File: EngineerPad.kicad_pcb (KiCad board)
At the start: 2 copper layers, 114.9 x 97.8 mm, 69 parts, among them J1 AVR ISP, J2 USB_A, SW1 SW_Push, SW10 SW_Push, SW11 SW_Push, SW12 SW_Push, SW13 SW_Push, SW14 SW_Push, SW15 SW_Push, SW16 SW_Push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

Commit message: wip
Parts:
- moved C3 0.63 mm to (187.5, 79.8)
- moved F1 0.23 mm to (181.9, 79.9)
- moved D24 0.21 mm to (174.8, 81.1)
- moved D25 0.21 mm to (178.0, 81.1)
- moved D26 0.21 mm to (187.5, 73.5)
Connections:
- J1 pad 1: Row1 -> Col1
- J1 pad 3: Row0 -> Col0
- J1 pad 4: Row2 -> Col2
- U1 pad 15: Row0 -> Col4
- U1 pad 16: Row1 -> Col3
- U1 pad 17: Row2 -> Col2
- U1 pad 18: Row3 -> Col1
- U1 pad 19: Row4 -> Col0
- U1 pad 23: Col4 -> Row0
- U1 pad 24: Col3 -> Row1
- U1 pad 25: Col2 -> Row2
- U1 pad 26: Col1 -> Row3
- U1 pad 27: Col0 -> Row4
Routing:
- net +5V: track 0.00 -> 117.9 mm
- net Reset: track 0.00 -> 84.9 mm
- net D+: track 0.00 -> 33.8 mm
- net D-: track 0.00 -> 30.0 mm
- net /DN: track 0.00 -> 22.4 mm
- net /DP: track 0.00 -> 19.7 mm
- net Net-(C1-Pad2): track 0.00 -> 11.4 mm
- net Net-(C2-Pad2): track 0.00 -> 10.2 mm
- net Net-(F1-Pad2): track 0.00 -> 6.88 mm

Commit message: handwired
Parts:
- moved D23 0.20 mm to (152.0, 138.9)
- moved D21 0.20 mm to (133.0, 138.9)
- moved U1 0.18 mm to (182.5, 128.1)
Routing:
- net Col2: track 0.00 -> 200.3 mm
- net Col0: track 0.00 -> 193.5 mm
- net Col1: track 0.00 -> 181.0 mm
- net Row0: track 0.00 -> 129.9 mm
- net Col3: track 0.00 -> 126.8 mm
- net Col4: track 0.00 -> 114.3 mm
- net Row1: track 0.00 -> 109.4 mm
- net Row3: track 0.00 -> 99.4 mm
- net Row2: track 0.00 -> 94.6 mm
- net Row4: track 0.00 -> 63.2 mm
- net Net-(D21-Pad2): track 0.00 -> 16.4 mm
- net Net-(D19-Pad2): track 0.00 -> 12.6 mm
- net Net-(D4-Pad2): track 0.00 -> 12.6 mm
- net Net-(D14-Pad2): track 0.00 -> 12.6 mm
- net Net-(D16-Pad2): track 0.00 -> 12.6 mm
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
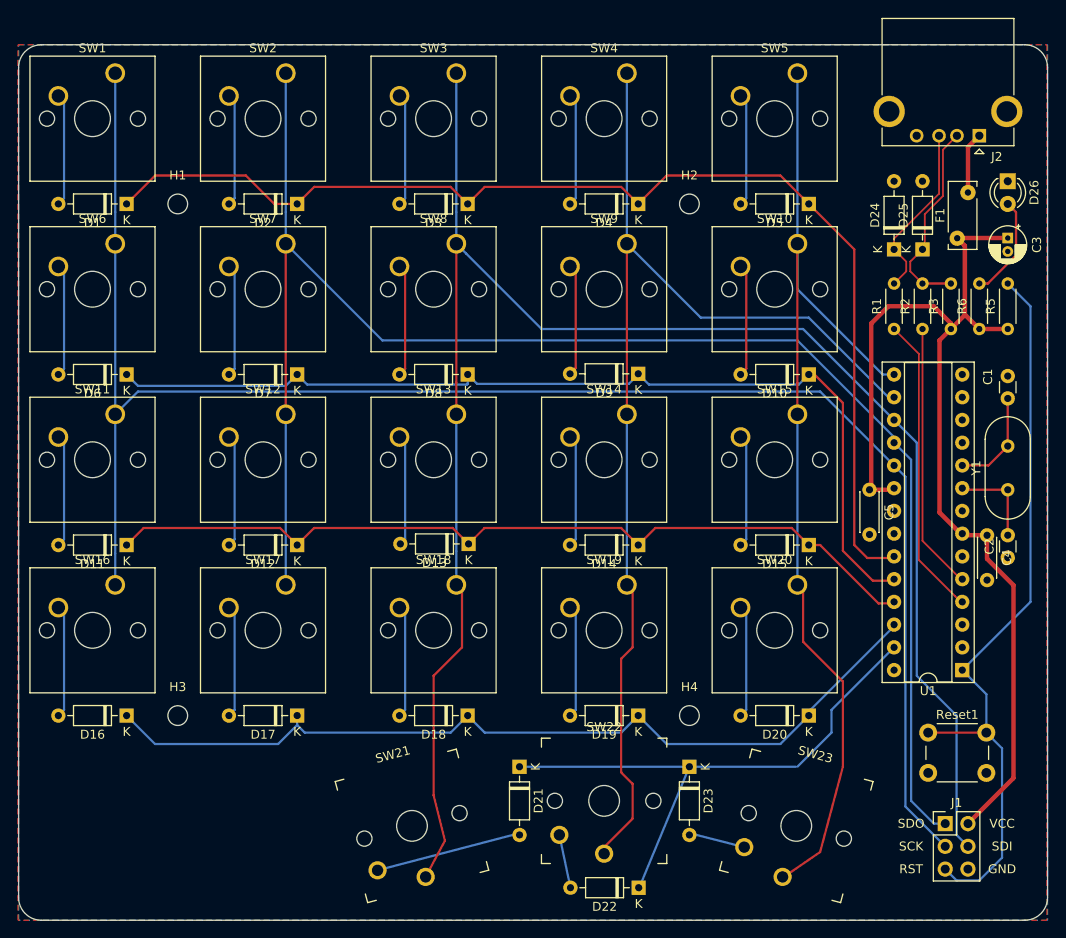
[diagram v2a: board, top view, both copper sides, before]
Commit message: fix minor wiring
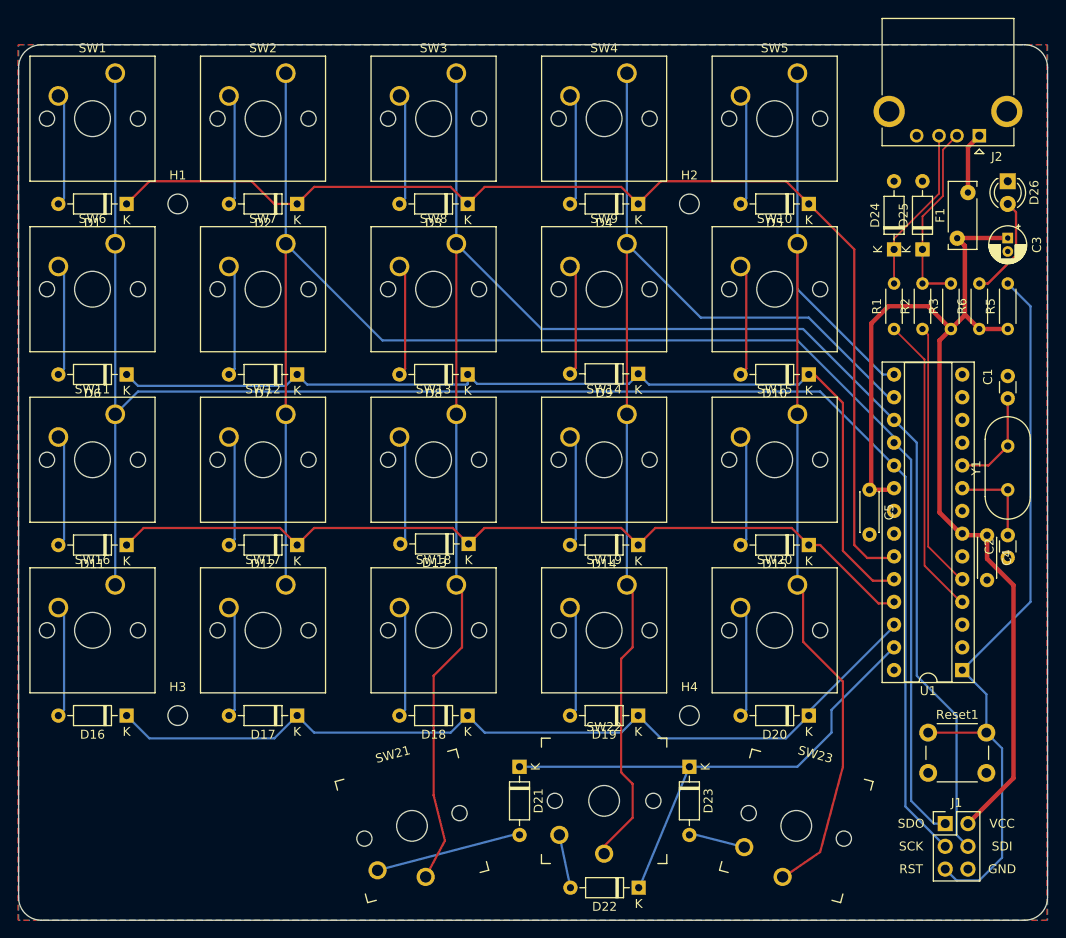
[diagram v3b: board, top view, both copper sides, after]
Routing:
- net Row3: track 99.4 -> 97.5 mm
- net /DP: track 19.7 -> 18.6 mm
- net /DN: track 22.4 -> 21.3 mm
- net Row0: track 129.9 -> 128.8 mm
- net +5V: track 118.4 -> 117.4 mm

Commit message: working version
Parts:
- D1, D10, D11, D12, D13, D14, D15, D16, D17, D18, D19, D2, D20, D21, D22, D23, D3, D4, D5, D6, D7, D8, D9: footprint Diode_THT:D_DO-35_SOD27_P7.62mm_Horizontal -> JSA:D_DO-35_SOD27_P7.62mm_Horizontal
- J1: value AVR ISP -> AVR ISP 6
- SW1, SW10, SW11, SW12, SW13, SW14, SW15, SW16, SW17, SW18, SW19, SW2, SW20, SW3, SW4, SW5, SW6, SW7, SW8, SW9: footprint Button_Switch_Keyboard:SW_Cherry_MX_1.00u_PCB -> JSA:SW_Cherry_MX_1.00u_PCB

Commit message: silkscreen improvent
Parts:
- C2: value 22pf -> 22pF
- C3: value 4.7u -> 4.7μF
- C4, C5: value 0.1u -> 0.1μF
- J1: value AVR ISP 6 -> AVR ISP
- R1, R2: value 75 -> 75Ω
- R3: value 1.5k -> 1.5kΩ
- R5: value 10k -> 10kΩ
- R6: value 1.5K -> 1.5kΩ
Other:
- board text added: "Zenner Diode"

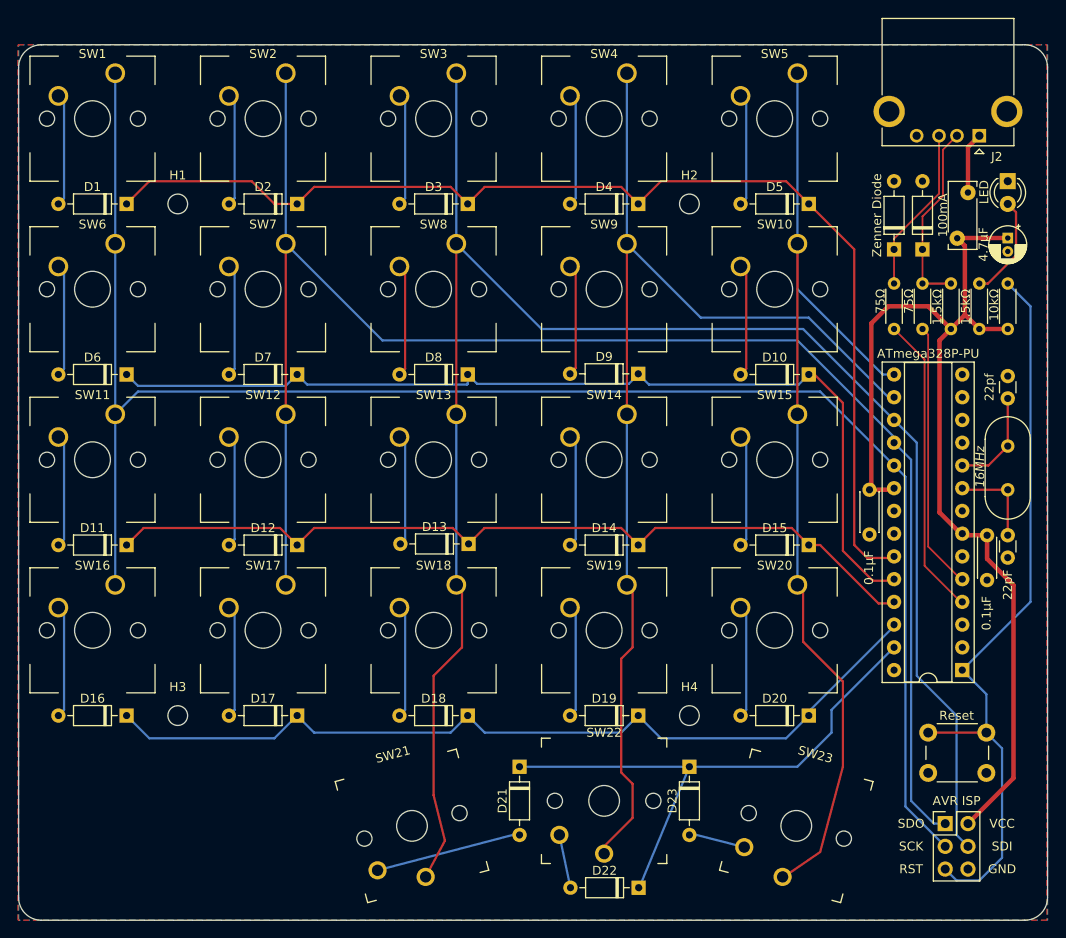
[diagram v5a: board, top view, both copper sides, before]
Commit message: silkscreen and aref to ground
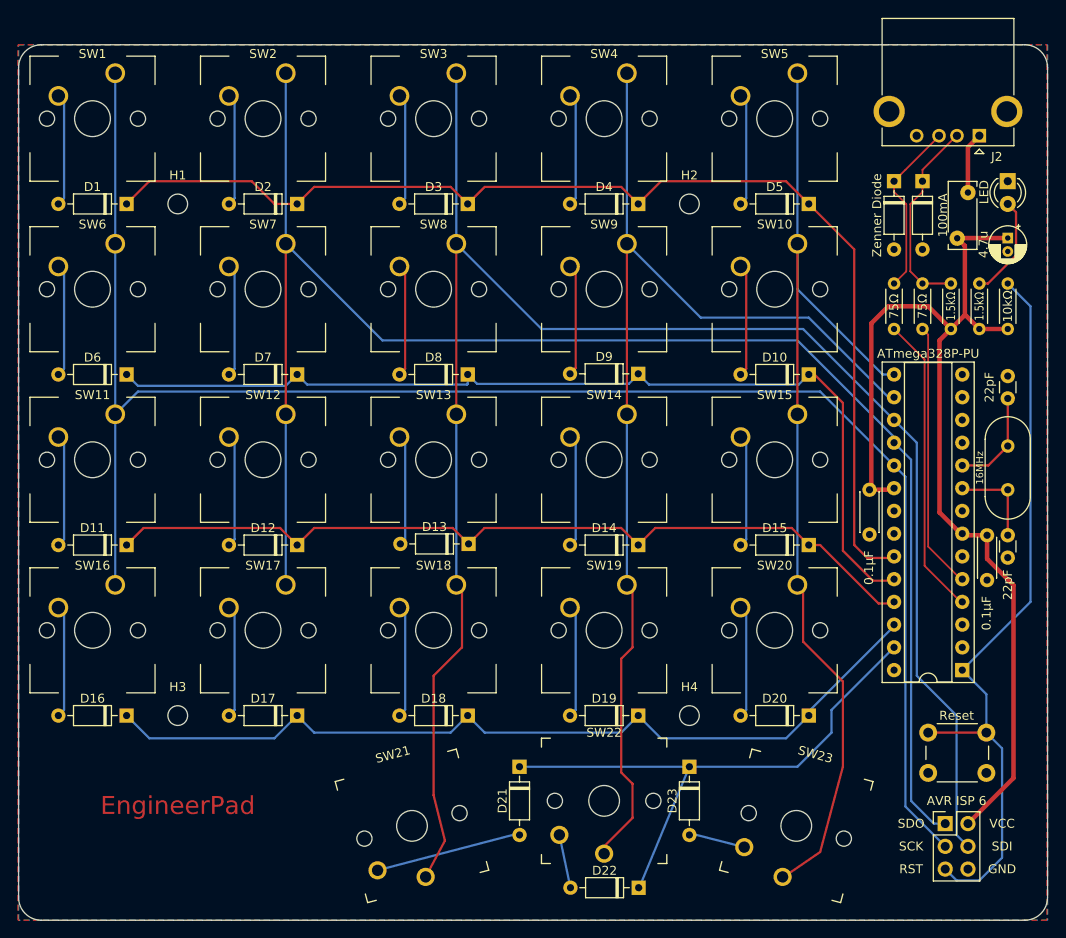
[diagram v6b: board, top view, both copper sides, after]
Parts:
- added REF**: OSHW-Logo2_36.5x30mm_SilkScreen, Symbol:OSHW-Logo2_36.5x30mm_SilkScreen, B.Cu at (94.8, 135.6)
- added REF**: KiCad-Logo_20mm_SilkScreen, Symbol:KiCad-Logo_20mm_SilkScreen, B.Cu at (142.3, 132.5)
- C1: value 22pf -> 22pF
- C3: value 4.7μF -> 4.7u
- J1: value AVR ISP -> AVR ISP 6
- moved D24 7.62 mm to (174.8, 73.5), turned to 270 degrees
- moved D25 7.62 mm to (178.0, 73.5), turned to 270 degrees
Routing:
- net /DN: track 21.3 -> 22.4 mm
- net /DP: track 18.6 -> 19.7 mm
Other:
- board text added: "EngineerPad"
- board text added: "Powered by"
- board text added: "Rev 0.3 2020-9-2 James Sa"

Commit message: remove aref add a logo
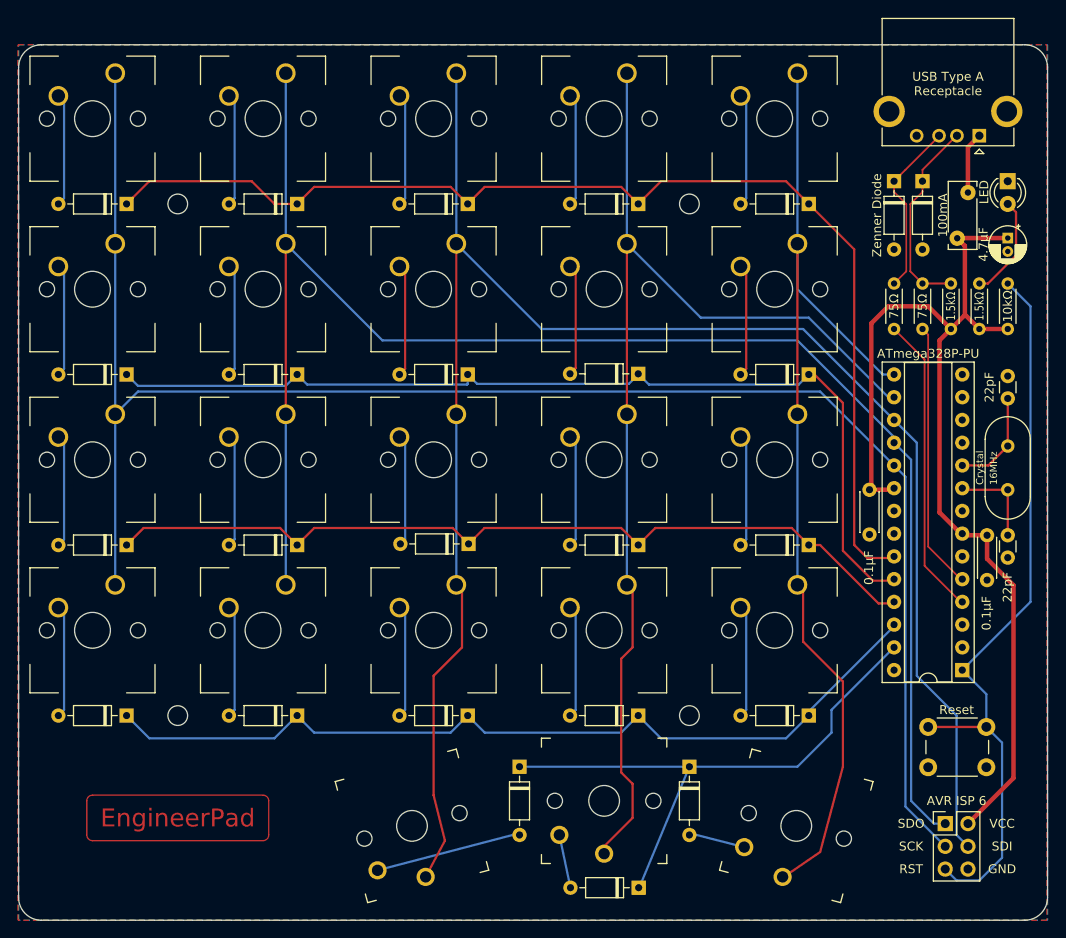
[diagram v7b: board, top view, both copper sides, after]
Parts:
- removed REF**: OSHW-Logo2_36.5x30mm_SilkScreen, Symbol:OSHW-Logo2_36.5x30mm_SilkScreen
- removed REF**: KiCad-Logo_20mm_SilkScreen, Symbol:KiCad-Logo_20mm_SilkScreen
- added Logo_KiCad: KiCad-Logo_20mm_SilkScreen, Symbol:KiCad-Logo_20mm_SilkScreen, B.Cu at (138.5, 132.2)
- added OSHW_Logo: OSHW-Logo2_36.5x30mm_SilkScreen, Symbol:OSHW-Logo2_36.5x30mm_SilkScreen, B.Cu at (94.8, 135.5)
- C3: value 4.7u -> 4.7μF
- D1, D10, D11, D12, D13, D14, D15, D16, D17, D18, D19, D2, D20, D21, D22, D23, D3, D4, D5, D6, D7, D8, D9: footprint JSA:D_DO-35_SOD27_P7.62mm_Horizontal -> JSA:Diode_THT
- SW21, SW22, SW23: value SW_Push -> PG1350
- moved R2 5.08 mm to (178.0, 84.9), turned to 270 degrees
- moved Reset1 0.64 mm to (178.6, 134.4)
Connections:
- R2 pad 1: D- -> /DN
- R2 pad 2: /DN -> D-
- U1 pad 11: Net-(U1-Pad11) -> (no net)
- U1 pad 12: Net-(U1-Pad12) -> (no net)
- U1 pad 13: Net-(U1-Pad13) -> (no net)
- U1 pad 14: Net-(U1-Pad14) -> (no net)
- U1 pad 2: Net-(U1-Pad2) -> (no net)
- U1 pad 21: Net-(U1-Pad21) -> (no net)
- U1 pad 28: Net-(U1-Pad28) -> (no net)
- U1 pad 3: Net-(U1-Pad3) -> (no net)
- U1 pad 6: Net-(U1-Pad6) -> (no net)
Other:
- board text added: "Crystal"
- board text added: "Design with"
- board text added: "Rev 0.3 Sep 2020 James Sa"
- board text added: "USB Type A Receptacle"
- board text removed: "Powered by"
- board text removed: "Rev 0.3 2020-9-2 James Sa"
